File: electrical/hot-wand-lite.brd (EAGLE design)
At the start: 112 x 72 mm, 90 parts, among them IC1 12V R-78K12-2.0, IC2 AMS1117-5.0, Q1 NCHAN, Q2 SIS862ADN-T1-GE3, Q3 DMTH64M2LPDWQ-13, Q4 2N7002K, Q5 SIS862ADN-T1-GE3, U1 SEEED-XIAO-SAMD21-TH-LOCKING, U2 1EDN8511BXUSA1, U3 LM74700QDBVTQ1, U4 AP53781

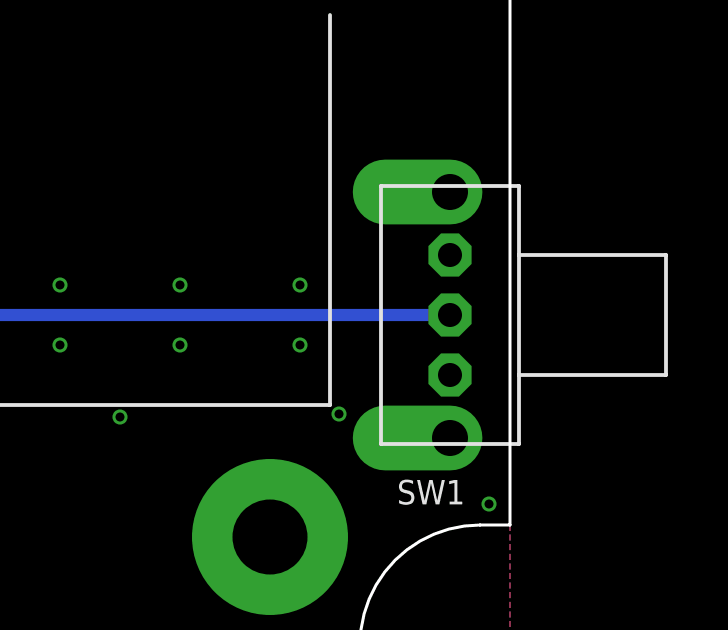
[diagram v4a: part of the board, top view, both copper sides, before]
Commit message: update gate resistors for higher wattage
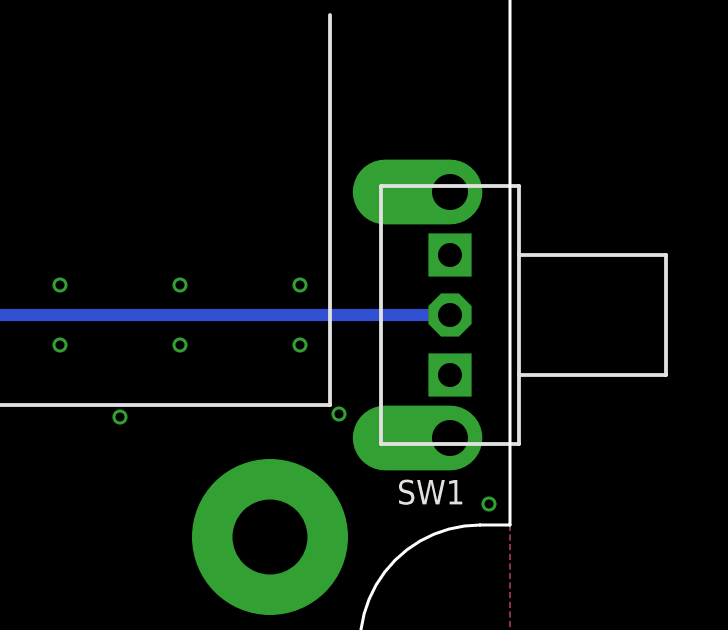
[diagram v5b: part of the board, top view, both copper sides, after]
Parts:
- SW1: value (none) -> SWITCH-SPDT-2MNT-SLW-864574-5A-RA-N-D
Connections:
- net GND: no longer SW1.R
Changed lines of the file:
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@@
 </element>
 <element name="R3" library="hot-wand" package="0603-RES" value="3R6" x="45.4" y="68.6" smashed="yes" rot="MR0">
-<attribute name="JLCPARTNUM" value="C54921041" x="45.4" y="68.6" size="1.778" layer="28" rot="MR0" display="off"/>
+<attribute name="JLCPARTNUM" value="C445783" x="45.4" y="68.6" size="1.778" layer="28" rot="MR0" display="off"/>
 <attribute name="NAME" x="43.589" y="68.262" size="0.8128" layer="26" font="fixed" rot="MR0"/>
 <attribute name="VALUE" x="44.616" y="69.457" size="0.8128" layer="28" font="vector" rot="MR0"/>
@@
 </element>
 <element name="R4" library="hot-wand" package="0603-RES" value="3R6" x="48.8" y="69.7" smashed="yes" rot="MR0">
-<attribute name="JLCPARTNUM" value="C54921041" x="48.8" y="69.7" size="1.778" layer="28" rot="MR0" display="off"/>
+<attribute name="JLCPARTNUM" value="C445783" x="48.8" y="69.7" size="1.778" layer="28" rot="MR0" display="off"/>
 <attribute name="NAME" x="47.089" y="69.462" size="0.8128" layer="26" font="fixed" rot="MR0"/>
 <attribute name="VALUE" x="47.384" y="68.943" size="0.8128" layer="28" font="vector" rot="MR180"/>
@@
 <attribute name="VALUE" x="98.316" y="51.257" size="0.8128" layer="28" font="vector" rot="MR0"/>
 </element>
-<element name="SW1" library="hot-wand" package="SWITCH-SLW-864574-5A-RA-N-D" value="" x="110" y="12" smashed="yes" rot="R270">
+<element name="SW1" library="hot-wand" package="SWITCH-SLW-864574-5A-RA-N-D" value="SWITCH-SPDT-2MNT-SLW-864574-5A-RA-N-D" x="110" y="12" smashed="yes" rot="R270">
 <attribute name="NAME" x="110.5" y="6.5" size="0.8128" layer="25" rot="R180"/>
 <attribute name="JLC-DNP" value="1" x="110" y="12" size="1.778" layer="27" rot="R270" display="off"/>
@@
 <via x="14.6" y="28.2" extent="1-16" drill="0.3" shape="octagon"/>
 <via x="9.2" y="29.9" extent="1-16" drill="0.3" shape="octagon"/>
-<contactref element="SW1" pad="R"/>
 <contactref element="SW1" pad="M1"/>
 <contactref element="SW1" pad="M2"/>

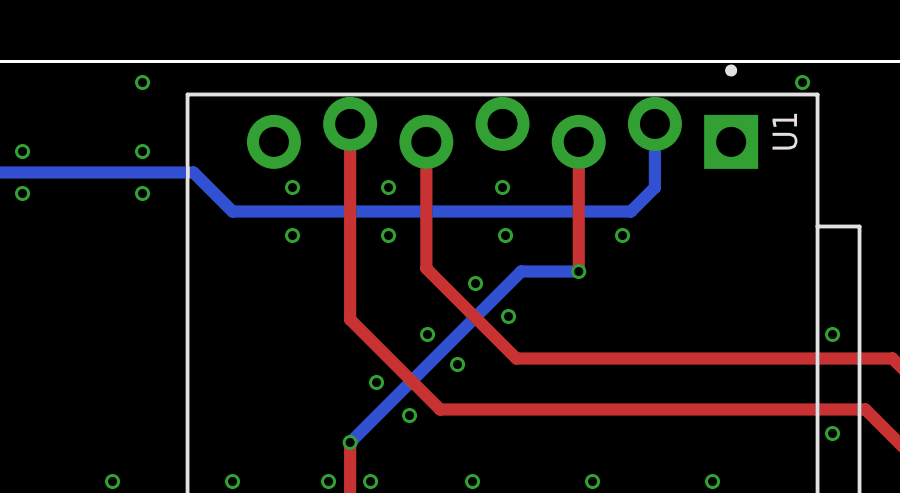
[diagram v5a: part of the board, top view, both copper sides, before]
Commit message: slight design changes in response to sergeymax's video
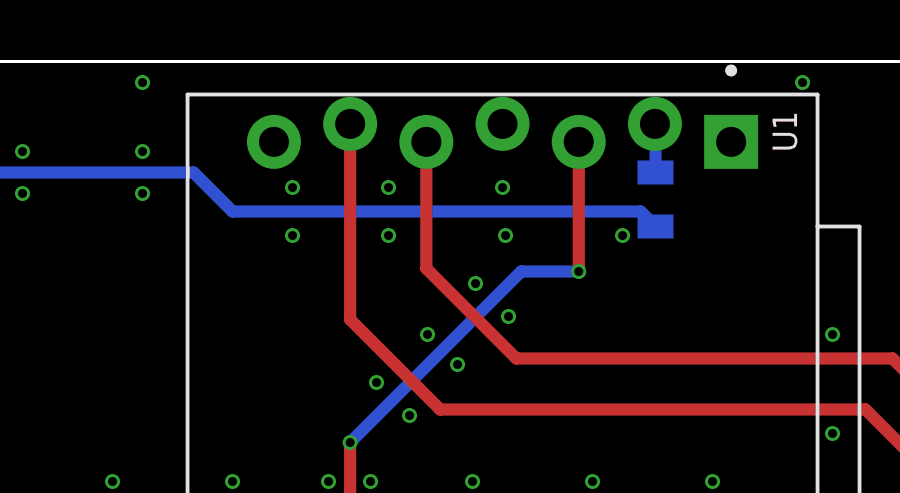
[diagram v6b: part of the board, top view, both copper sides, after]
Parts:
- added R26: 100Ω, hot-wand:0805
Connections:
- new net RF-GEN-: R26.2, U1.2
- net RF-GEN: now also R26.1; no longer U1.2
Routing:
- net RF-GEN: track 34.2 -> 31.9 mm
- net RF-GEN-: track 0.00 -> 1.63 mm
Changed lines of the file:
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@@
 <attribute name="PARTNUM" value="SLW-864574-5A-RA-N-D" x="110" y="12" size="1.778" layer="27" rot="R270" display="off"/>
+</element>
+<element name="R26" library="hot-wand" package="0805" value="100Ω" x="93.1" y="67.4" smashed="yes" rot="MR90">
+<attribute name="JLCPARTNUM" value="C441975" x="93.1" y="67.4" size="0.8128" layer="28" rot="MR90" display="off"/>
+<attribute name="NAME" x="94.0255" y="65.738" size="0.8128" layer="26" rot="MR90"/>
+<attribute name="VALUE" x="95.003" y="65.084" size="0.8128" layer="28" rot="MR90"/>
 </element>
 </elements>
@@
 <signal name="RF-GEN">
 <contactref element="R1" pad="1"/>
-<contactref element="U1" pad="2"/>
-<wire x1="79" y1="67" x2="92.28" y2="67" width="0.4064" layer="16"/>
-<wire x1="92.28" y1="67" x2="93.08" y2="67.8" width="0.4064" layer="16"/>
-<wire x1="93.08" y1="67.8" x2="93.08" y2="69.92" width="0.4064" layer="16"/>
+<wire x1="79" y1="67" x2="92.6" y2="67" width="0.4064" layer="16"/>
 <wire x1="79" y1="67" x2="77.7" y2="68.3" width="0.4064" layer="16"/>
 <wire x1="77.7" y1="68.3" x2="61.9" y2="68.3" width="0.4064" layer="16"/>
+<contactref element="R26" pad="1"/>
+<wire x1="92.6" y1="67" x2="93.1" y2="66.5" width="0.4064" layer="16"/>
 </signal>
 <signal name="12V-2">
@@
 <wire x1="98.05" y1="41" x2="98.05" y2="49.5" width="0.4064" layer="16"/>
 </signal>
+<signal name="RF-GEN-">
+<contactref element="U1" pad="2"/>
+<contactref element="R26" pad="2"/>
+<wire x1="93.1" y1="68.3" x2="93.1" y2="69.9" width="0.4064" layer="16"/>
+<wire x1="93.1" y1="69.9" x2="93.08" y2="69.92" width="0.4064" layer="16"/>
+</signal>
 </signals>

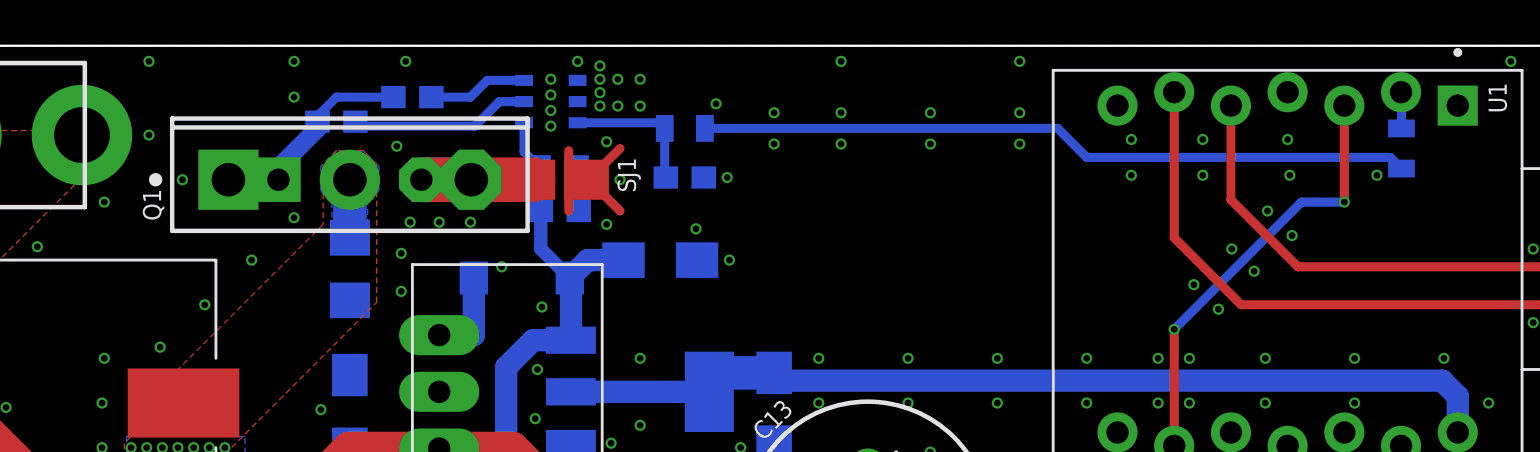
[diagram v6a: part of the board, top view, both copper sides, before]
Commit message: MOSFETs closer to enclosure wall for heat sink purposes
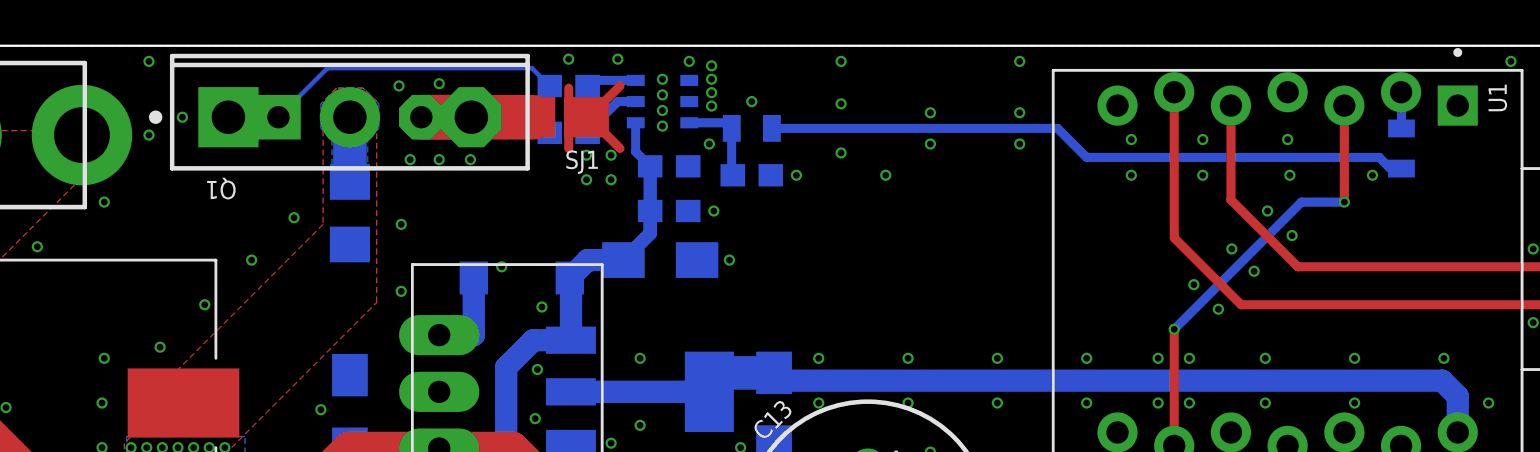
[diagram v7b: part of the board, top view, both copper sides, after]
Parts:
- moved R3 10.4 mm to (55.8, 68.1)
- moved R4 7.02 mm to (55.8, 70.2)
- moved C18 5.00 mm to (60.3, 66.6)
- moved U2 5.00 mm to (60.0, 69.5)
- moved C19 4.90 mm to (60.3, 64.6)
- moved R2 3.00 mm to (64.0, 66.2)
- moved R1 3.00 mm to (64.0, 68.3)
- moved Q1 2.80 mm to (46.0, 68.8)
- moved SJ1 2.80 mm to (55.4, 68.8)
- moved C1 2.50 mm to (46.0, 64.5)
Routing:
- net FET-GATE: track 9.57 -> 17.7 mm
- net N$14: track 8.21 -> 2.75 mm
- net RF-GEN: track 31.9 -> 28.9 mm
- net MCU-RF: track 6.51 -> 4.27 mm
- net N$15: track 4.46 -> 2.25 mm
- net +12V: track 92.9 -> 92.0 mm
- net GND: vias 376 -> 373
